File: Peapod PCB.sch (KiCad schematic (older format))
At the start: 17 parts, among them J1 CONN_01X01, J2 CONN_01X02, J3 CONN_01X01, J4 CONN_01X01, J5 CONN_01X01, J6 CONN_01X01, J7 CONN_01X02, U1 ESP8266

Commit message: Updated schematic
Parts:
- removed J3, J4: CONN_01X01, mod:Alligator Pad, symbol CONN_01X01
- added J3: CONN_01X06, Pin_Headers:Pin_Header_Straight_1x06_Pitch2.54mm, symbol CONN_01X06
- R3, R5: footprint (none) -> Resistors_SMD:R_0805_HandSoldering
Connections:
- net +3V3: now also J3.3 (P3)
- net GND: now also J3.1 (P1)
- net at U1.15 (RXD0): now also J3.4 (P4)
- net at U1.16 (TXD0): now also J3.5 (P5)
- no-connect marks 0 -> 2
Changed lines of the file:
@@
 $EndComp
 $Comp
-L GND #PWR5
+L GND #PWR01
 U 1 1 59932223
 P 4850 4225
-F 0 "#PWR5" H 4850 3975 50  0001 C CNN
+F 0 "#PWR01" H 4850 3975 50  0001 C CNN
 F 1 "GND" H 4850 4075 50  0000 C CNN
 F 2 "" H 4850 4225 50  0001 C CNN
@@
 $EndComp
 $Comp
-L GND #PWR6
+L GND #PWR02
 U 1 1 59932907
 P 6800 4100
-F 0 "#PWR6" H 6800 3850 50  0001 C CNN
+F 0 "#PWR02" H 6800 3850 50  0001 C CNN
 F 1 "GND" H 6800 3950 50  0000 C CNN
 F 2 "" H 6800 4100 50  0001 C CNN
@@
 $EndComp
 $Comp
-L GND #PWR1
+L GND #PWR03
 U 1 1 5993357D
 P 4500 3825
-F 0 "#PWR1" H 4500 3575 50  0001 C CNN
+F 0 "#PWR03" H 4500 3575 50  0001 C CNN
 F 1 "GND" H 4500 3675 50  0000 C CNN
 F 2 "" H 4500 3825 50  0001 C CNN
 F 3 "" H 4500 3825 50  0001 C CNN
 	1    4500 3825
-	1    0    0    -1
-$EndComp
-$Comp
-L CONN_01X01 J3
-U 1 1 59933B2D
-P 7450 2875
-F 0 "J3" H 7450 2975 50  0000 C CNN
-F 1 "CONN_01X01" V 7550 2875 50  0000 C CNN
-F 2 "mod:Alligator Pad" H 7450 2875 50  0001 C CNN
-F 3 "" H 7450 2875 50  0001 C CNN
-	1    7450 2875
-	1    0    0    -1
-$EndComp
-$Comp
-L CONN_01X01 J4
-U 1 1 59933BB9
-P 7450 3025
-F 0 "J4" H 7450 3125 50  0000 C CNN
-F 1 "CONN_01X01" V 7550 3025 50  0000 C CNN
-F 2 "mod:Alligator Pad" H 7450 3025 50  0001 C CNN
-F 3 "" H 7450 3025 50  0001 C CNN
-	1    7450 3025
 	1    0    0    -1
 $EndComp
@@
 $EndComp
 $Comp
-L +3.3V #PWR2
+L +3.3V #PWR04
 U 1 1 59933FE4
 P 5300 3175
-F 0 "#PWR2" H 5300 3025 50  0001 C CNN
+F 0 "#PWR04" H 5300 3025 50  0001 C CNN
 F 1 "+3.3V" H 5300 3315 50  0000 C CNN
 F 2 "" H 5300 3175 50  0001 C CNN
@@
 $EndComp
 $Comp
-L +3.3V #PWR4
+L +3.3V #PWR05
 U 1 1 59934256
 P 4950 3925
-F 0 "#PWR4" H 4950 3775 50  0001 C CNN
+F 0 "#PWR05" H 4950 3775 50  0001 C CNN
 F 1 "+3.3V" H 4950 4065 50  0000 C CNN
 F 2 "" H 4950 3925 50  0001 C CNN
@@
 	4500 3775 5050 3775
 Wire Wire Line
-	4500 3475 4500 3625
-Wire Wire Line
-	4500 3625 4500 3775
-Wire Wire Line
-	4500 3775 4500 3825
+	4500 3475 4500 3825
 Connection ~ 4500 3625
 Wire Wire Line
@@
 Wire Wire Line
 	6625 3325 7250 3325
-Wire Wire Line
-	6625 2875 7250 2875
-Wire Wire Line
-	6625 3025 7250 3025
 Wire Wire Line
 	4500 3475 5050 3475
@@
 	4950 4225 4850 4225
 Wire Wire Line
-	5125 2700 5125 2875
-Wire Wire Line
-	5125 2875 5125 3325
+	5125 2700 5125 3325
 Wire Wire Line
 	5125 2875 5325 2875
 Connection ~ 5125 2875
 Wire Wire Line
-	4825 3025 4875 3025
-Wire Wire Line
-	4875 3025 5325 3025
+	4825 3025 5325 3025
 $Comp
 L R R2
@@
 $EndComp
 Wire Wire Line
-	6625 3475 7100 3475
-Wire Wire Line
-	7100 3475 7250 3475
+	6625 3475 7250 3475
 Connection ~ 7100 3475
 $Comp
@@
 $EndComp
 $Comp
-L GND #PWR3
+L GND #PWR06
 U 1 1 599363AF
 P 5325 2700
-F 0 "#PWR3" H 5325 2450 50  0001 C CNN
+F 0 "#PWR06" H 5325 2450 50  0001 C CNN
 F 1 "GND" H 5325 2550 50  0000 C CNN
 F 2 "" H 5325 2700 50  0001 C CNN
@@
 $EndComp
 $Comp
-L +3.3V #PWR7
+L +3.3V #PWR07
 U 1 1 599466C8
 P 7100 3875
-F 0 "#PWR7" H 7100 3725 50  0001 C CNN
+F 0 "#PWR07" H 7100 3725 50  0001 C CNN
 F 1 "+3.3V" H 7100 4015 50  0000 C CNN
 F 2 "" H 7100 3875 50  0001 C CNN
@@
 F 0 "R3" V 6905 3625 50  0000 C CNN
 F 1 "10k" V 6825 3625 50  0000 C CNN
-F 2 "" V 6755 3625 50  0001 C CNN
+F 2 "Resistors_SMD:R_0805_HandSoldering" V 6755 3625 50  0001 C CNN
 F 3 "" H 6825 3625 50  0001 C CNN
 	1    6825 3625
@@
 F 0 "R5" V 6880 3925 50  0000 C CNN
 F 1 "10k" V 6800 3925 50  0000 C CNN
-F 2 "" V 6730 3925 50  0001 C CNN
+F 2 "Resistors_SMD:R_0805_HandSoldering" V 6730 3925 50  0001 C CNN
 F 3 "" H 6800 3925 50  0001 C CNN
 	1    6800 3925
@@
 	6625 3775 6800 3775
 $Comp
-L +3.3V #PWR?
+L +3.3V #PWR08
 U 1 1 59948486
 P 6975 3700
-F 0 "#PWR?" H 6975 3550 50  0001 C CNN
+F 0 "#PWR08" H 6975 3550 50  0001 C CNN
 F 1 "+3.3V" H 6975 3840 50  0000 C CNN
 F 2 "" H 6975 3700 50  0001 C CNN
@@
 	4875 2900 4875 3025
 $Comp
-L GND #PWR?
+L GND #PWR09
 U 1 1 5994872F
 P 4875 2525
-F 0 "#PWR?" H 4875 2275 50  0001 C CNN
+F 0 "#PWR09" H 4875 2275 50  0001 C CNN
 F 1 "GND" H 4875 2375 50  0000 C CNN
 F 2 "" H 4875 2525 50  0001 C CNN
@@
 	4875 2525 4875 2600
 $Comp
-L GND #PWR?
+L GND #PWR010
 U 1 1 599488CC
 P 7250 3750
-F 0 "#PWR?" H 7250 3500 50  0001 C CNN
+F 0 "#PWR010" H 7250 3500 50  0001 C CNN
 F 1 "GND" H 7250 3600 50  0000 C CNN
 F 2 "" H 7250 3750 50  0001 C CNN
@@
 $EndComp
 $Comp
-L GND #PWR?
+L GND #PWR011
 U 1 1 59948924
 P 6625 4000
-F 0 "#PWR?" H 6625 3750 50  0001 C CNN
+F 0 "#PWR011" H 6625 3750 50  0001 C CNN
 F 1 "GND" H 6625 3850 50  0000 C CNN
 F 2 "" H 6625 4000 50  0001 C CNN
@@
 Wire Wire Line
 	5325 3925 4950 3925
+$Comp
+L CONN_01X06 J3
+U 1 1 59947FD8
+P 7500 2450
+F 0 "J3" H 7500 2800 50  0000 C CNN
+F 1 "CONN_01X06" V 7600 2450 50  0000 C CNN
+F 2 "Pin_Headers:Pin_Header_Straight_1x06_Pitch2.54mm" H 7500 2450 50  0001 C CNN
+F 3 "" H 7500 2450 50  0001 C CNN
+	1    7500 2450
+	1    0    0    -1
+$EndComp
+$Comp
+L GND #PWR012
+U 1 1 599480D5
+P 6875 2200
+F 0 "#PWR012" H 6875 1950 50  0001 C CNN
+F 1 "GND" H 6875 2050 50  0000 C CNN
+F 2 "" H 6875 2200 50  0001 C CNN
+F 3 "" H 6875 2200 50  0001 C CNN
+	1    6875 2200
+	0    1    1    0
+$EndComp
+Wire Wire Line
+	6875 2200 7300 2200
+$Comp
+L +3.3V #PWR013
+U 1 1 599481A2
+P 6850 2400
+F 0 "#PWR013" H 6850 2250 50  0001 C CNN
+F 1 "+3.3V" H 6850 2540 50  0000 C CNN
+F 2 "" H 6850 2400 50  0001 C CNN
+F 3 "" H 6850 2400 50  0001 C CNN
+	1    6850 2400
+	0    -1   -1   0
+$EndComp
+Wire Wire Line
+	6850 2400 7300 2400
+Wire Wire Line
+	6625 2875 6800 2875
+Wire Wire Line
+	6800 2875 6800 2600
+Wire Wire Line
+	6800 2600 7300 2600
+Wire Wire Line
+	6625 3025 6625 2500
+Wire Wire Line
+	6625 2500 7300 2500
+NoConn ~ 7300 2700
+NoConn ~ 7300 2300
 $EndSCHEMATC

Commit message: Updated lib
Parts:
- BTN1, BTN3, BTN4: symbol Pushbutton -> Pushbutton-RESCUE-Peapod_PCB
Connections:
- net GND: now also BTN1.~, BTN3.~, BTN4.~; no longer BTN1.1, BTN3.1, BTN4.1
- net at U1.5 (GPIO14): now also BTN4.~; no longer BTN4.2
- net at U1.6 (GPIO12): now also BTN3.~; no longer BTN3.2
- net at U1.7 (GPIO13): now also BTN1.~; no longer BTN1.2
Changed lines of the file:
@@
 EESchema Schematic File Version 2
+LIBS:Peapod PCB-rescue
 LIBS:power
 LIBS:device
@@
 $EndComp
 $Comp
-L Pushbutton BTN1
+L Pushbutton-RESCUE-Peapod_PCB BTN1
 U 1 1 5993320C
 P 5150 3775
@@
 $EndComp
 $Comp
-L Pushbutton BTN3
+L Pushbutton-RESCUE-Peapod_PCB BTN3
 U 1 1 599332EE
 P 4775 3625
@@
 $EndComp
 $Comp
-L Pushbutton BTN4
+L Pushbutton-RESCUE-Peapod_PCB BTN4
 U 1 1 5993333F
 P 5150 3475

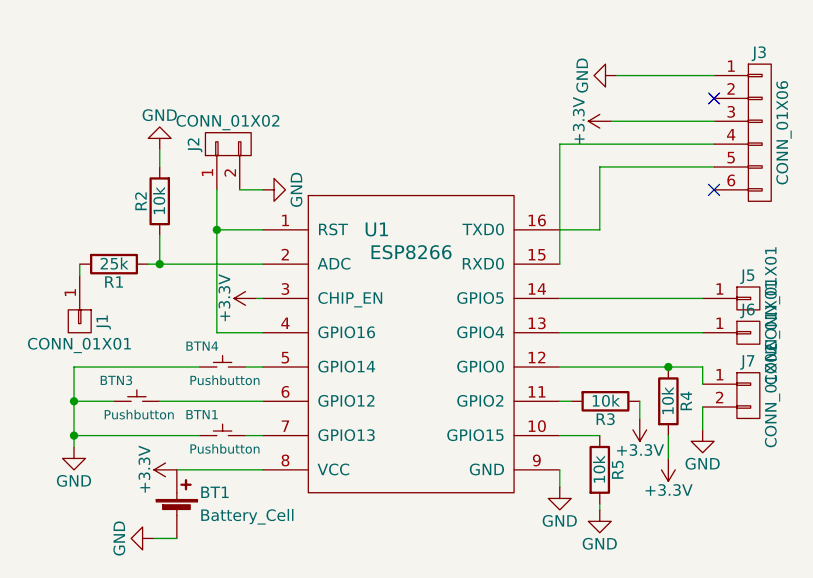
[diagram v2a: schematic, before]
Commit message: updated pushbutton
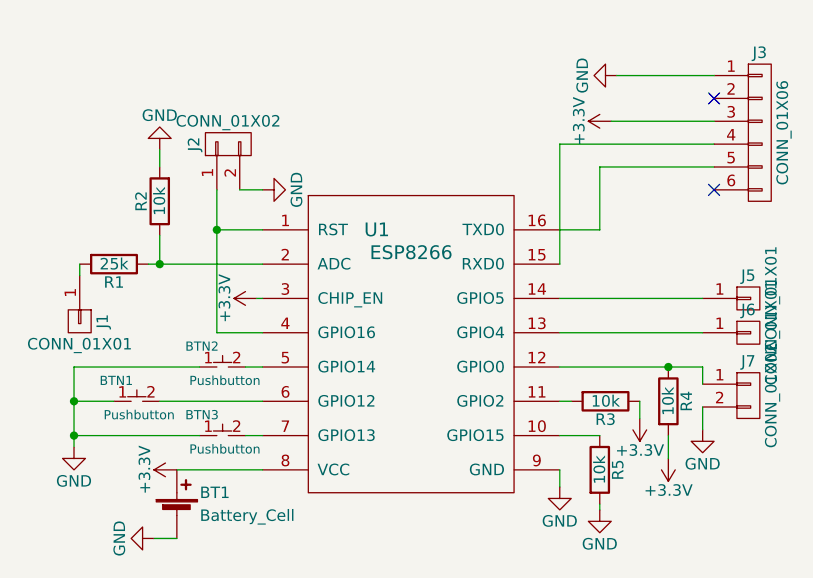
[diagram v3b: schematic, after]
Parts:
- removed BTN1, BTN3, BTN4: Pushbutton, mod:Pushbutton, symbol Pushbutton-RESCUE-Peapod_PCB
- added BTN1, BTN2, BTN3: Pushbutton, mod:Pushbutton, symbol Pushbutton
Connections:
- net GND: now also BTN1.1, BTN2.1, BTN3.1
- net at U1.5 (GPIO14): now also BTN2.2
- net at U1.6 (GPIO12): now also BTN1.2
- net at U1.7 (GPIO13): now also BTN3.2
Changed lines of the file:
@@
-$EndComp
-$Comp
-L Pushbutton-RESCUE-Peapod_PCB BTN1
-U 1 1 5993320C
-P 5150 3775
-F 0 "BTN1" H 5060 3865 40  0000 C CNN
-F 1 "Pushbutton" H 5160 3715 40  0000 C CNN
-F 2 "mod:Pushbutton" H 4850 3375 60  0001 C CNN
-F 3 "" H 4850 3375 60  0001 C CNN
-	1    5150 3775
-	1    0    0    -1
-$EndComp
-$Comp
-L Pushbutton-RESCUE-Peapod_PCB BTN3
-U 1 1 599332EE
-P 4775 3625
-F 0 "BTN3" H 4685 3715 40  0000 C CNN
-F 1 "Pushbutton" H 4785 3565 40  0000 C CNN
-F 2 "mod:Pushbutton" H 4475 3225 60  0001 C CNN
-F 3 "" H 4475 3225 60  0001 C CNN
-	1    4775 3625
-	1    0    0    -1
-$EndComp
-$Comp
-L Pushbutton-RESCUE-Peapod_PCB BTN4
-U 1 1 5993333F
-P 5150 3475
-F 0 "BTN4" H 5060 3565 40  0000 C CNN
-F 1 "Pushbutton" H 5160 3415 40  0000 C CNN
-F 2 "mod:Pushbutton" H 4850 3075 60  0001 C CNN
-F 3 "" H 4850 3075 60  0001 C CNN
-	1    5150 3475
-	1    0    0    -1
 $EndComp
 $Comp
@@
 NoConn ~ 7300 2700
 NoConn ~ 7300 2300
+$Comp
+L Pushbutton BTN2
+U 1 1 5994A123
+P 5150 3475
+F 0 "BTN2" H 5060 3565 40  0000 C CNN
+F 1 "Pushbutton" H 5160 3415 40  0000 C CNN
+F 2 "mod:Pushbutton" H 4850 3075 60  0001 C CNN
+F 3 "" H 4850 3075 60  0001 C CNN
+	1    5150 3475
+	1    0    0    -1
+$EndComp
+$Comp
+L Pushbutton BTN1
+U 1 1 5994A192
+P 4775 3625
+F 0 "BTN1" H 4685 3715 40  0000 C CNN
+F 1 "Pushbutton" H 4785 3565 40  0000 C CNN
+F 2 "mod:Pushbutton" H 4475 3225 60  0001 C CNN
+F 3 "" H 4475 3225 60  0001 C CNN
+	1    4775 3625
+	1    0    0    -1
+$EndComp
+$Comp
+L Pushbutton BTN3
+U 1 1 5994A1EB
+P 5150 3775
+F 0 "BTN3" H 5060 3865 40  0000 C CNN
+F 1 "Pushbutton" H 5160 3715 40  0000 C CNN
+F 2 "mod:Pushbutton" H 4850 3375 60  0001 C CNN
+F 3 "" H 4850 3375 60  0001 C CNN
+	1    5150 3775
+	1    0    0    -1
+$EndComp
 $EndSCHEMATC

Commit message: Changed schematic
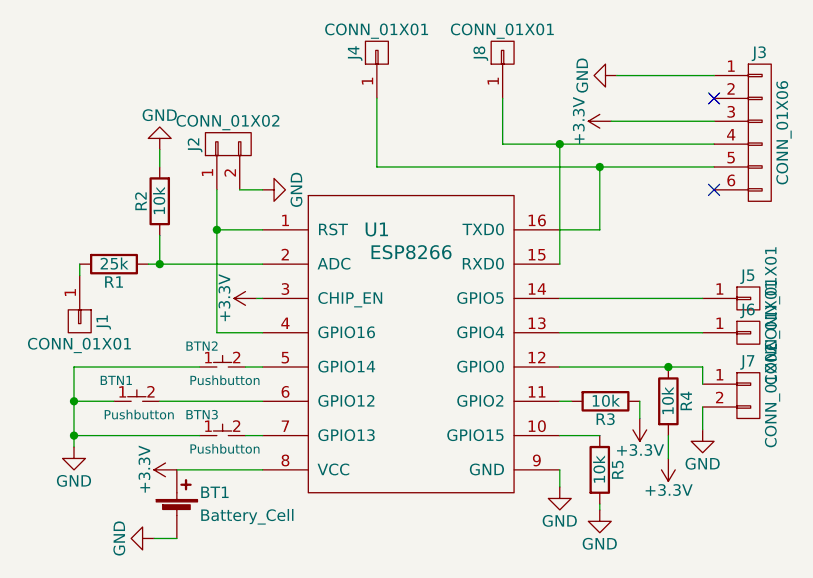
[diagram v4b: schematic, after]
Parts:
- added J4, J8: CONN_01X01, symbol CONN_01X01
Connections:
- net at J3.4 (P4), U1.15 (RXD0): now also J8.1 (P1)
- net at J3.5 (P5), U1.16 (TXD0): now also J4.1 (P1)
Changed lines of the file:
@@
 $EndComp
 $Comp
-L GND #PWR01
+L GND #PWR2
 U 1 1 59932223
 P 4850 4225
-F 0 "#PWR01" H 4850 3975 50  0001 C CNN
+F 0 "#PWR2" H 4850 3975 50  0001 C CNN
 F 1 "GND" H 4850 4075 50  0000 C CNN
 F 2 "" H 4850 4225 50  0001 C CNN
@@
 $EndComp
 $Comp
-L GND #PWR02
+L GND #PWR8
 U 1 1 59932907
 P 6800 4100
-F 0 "#PWR02" H 6800 3850 50  0001 C CNN
+F 0 "#PWR8" H 6800 3850 50  0001 C CNN
 F 1 "GND" H 6800 3950 50  0000 C CNN
 F 2 "" H 6800 4100 50  0001 C CNN
@@
 $EndComp
 $Comp
-L GND #PWR03
+L GND #PWR1
 U 1 1 5993357D
 P 4500 3825
-F 0 "#PWR03" H 4500 3575 50  0001 C CNN
+F 0 "#PWR1" H 4500 3575 50  0001 C CNN
 F 1 "GND" H 4500 3675 50  0000 C CNN
 F 2 "" H 4500 3825 50  0001 C CNN
@@
 $EndComp
 $Comp
-L +3.3V #PWR04
+L +3.3V #PWR5
 U 1 1 59933FE4
 P 5300 3175
-F 0 "#PWR04" H 5300 3025 50  0001 C CNN
+F 0 "#PWR5" H 5300 3025 50  0001 C CNN
 F 1 "+3.3V" H 5300 3315 50  0000 C CNN
 F 2 "" H 5300 3175 50  0001 C CNN
@@
 $EndComp
 $Comp
-L +3.3V #PWR05
+L +3.3V #PWR4
 U 1 1 59934256
 P 4950 3925
-F 0 "#PWR05" H 4950 3775 50  0001 C CNN
+F 0 "#PWR4" H 4950 3775 50  0001 C CNN
 F 1 "+3.3V" H 4950 4065 50  0000 C CNN
 F 2 "" H 4950 3925 50  0001 C CNN
@@
 	4500 3775 5050 3775
 Wire Wire Line
-	4500 3475 4500 3825
+	4500 3475 4500 3625
+Wire Wire Line
+	4500 3625 4500 3775
+Wire Wire Line
+	4500 3775 4500 3825
 Connection ~ 4500 3625
 Wire Wire Line
@@
 	4950 4225 4850 4225
 Wire Wire Line
-	5125 2700 5125 3325
+	5125 2700 5125 2875
+Wire Wire Line
+	5125 2875 5125 3325
 Wire Wire Line
 	5125 2875 5325 2875
 Connection ~ 5125 2875
 Wire Wire Line
-	4825 3025 5325 3025
+	4825 3025 4875 3025
+Wire Wire Line
+	4875 3025 5325 3025
 $Comp
 L R R2
@@
 $EndComp
 Wire Wire Line
-	6625 3475 7250 3475
+	6625 3475 7100 3475
+Wire Wire Line
+	7100 3475 7250 3475
 Connection ~ 7100 3475
 $Comp
@@
 $EndComp
 $Comp
-L GND #PWR06
+L GND #PWR6
 U 1 1 599363AF
 P 5325 2700
-F 0 "#PWR06" H 5325 2450 50  0001 C CNN
+F 0 "#PWR6" H 5325 2450 50  0001 C CNN
 F 1 "GND" H 5325 2550 50  0000 C CNN
 F 2 "" H 5325 2700 50  0001 C CNN
@@
 $EndComp
 $Comp
-L +3.3V #PWR07
+L +3.3V #PWR12
 U 1 1 599466C8
 P 7100 3875
-F 0 "#PWR07" H 7100 3725 50  0001 C CNN
+F 0 "#PWR12" H 7100 3725 50  0001 C CNN
 F 1 "+3.3V" H 7100 4015 50  0000 C CNN
 F 2 "" H 7100 3875 50  0001 C CNN
@@
 	6625 3775 6800 3775
 $Comp
-L +3.3V #PWR08
+L +3.3V #PWR11
 U 1 1 59948486
 P 6975 3700
-F 0 "#PWR08" H 6975 3550 50  0001 C CNN
+F 0 "#PWR11" H 6975 3550 50  0001 C CNN
 F 1 "+3.3V" H 6975 3840 50  0000 C CNN
 F 2 "" H 6975 3700 50  0001 C CNN
@@
 	4875 2900 4875 3025
 $Comp
-L GND #PWR09
+L GND #PWR3
 U 1 1 5994872F
 P 4875 2525
-F 0 "#PWR09" H 4875 2275 50  0001 C CNN
+F 0 "#PWR3" H 4875 2275 50  0001 C CNN
 F 1 "GND" H 4875 2375 50  0000 C CNN
 F 2 "" H 4875 2525 50  0001 C CNN
@@
 	4875 2525 4875 2600
 $Comp
-L GND #PWR010
+L GND #PWR13
 U 1 1 599488CC
 P 7250 3750
-F 0 "#PWR010" H 7250 3500 50  0001 C CNN
+F 0 "#PWR13" H 7250 3500 50  0001 C CNN
 F 1 "GND" H 7250 3600 50  0000 C CNN
 F 2 "" H 7250 3750 50  0001 C CNN
@@
 $EndComp
 $Comp
-L GND #PWR011
+L GND #PWR7
 U 1 1 59948924
 P 6625 4000
-F 0 "#PWR011" H 6625 3750 50  0001 C CNN
+F 0 "#PWR7" H 6625 3750 50  0001 C CNN
 F 1 "GND" H 6625 3850 50  0000 C CNN
 F 2 "" H 6625 4000 50  0001 C CNN
@@
 $EndComp
 $Comp
-L GND #PWR012
+L GND #PWR10
 U 1 1 599480D5
 P 6875 2200
-F 0 "#PWR012" H 6875 1950 50  0001 C CNN
+F 0 "#PWR10" H 6875 1950 50  0001 C CNN
 F 1 "GND" H 6875 2050 50  0000 C CNN
 F 2 "" H 6875 2200 50  0001 C CNN
@@
 	6875 2200 7300 2200
 $Comp
-L +3.3V #PWR013
+L +3.3V #PWR9
 U 1 1 599481A2
 P 6850 2400
-F 0 "#PWR013" H 6850 2250 50  0001 C CNN
+F 0 "#PWR9" H 6850 2250 50  0001 C CNN
 F 1 "+3.3V" H 6850 2540 50  0000 C CNN
 F 2 "" H 6850 2400 50  0001 C CNN
@@
 	6800 2875 6800 2600
 Wire Wire Line
+	6800 2600 6800 2600
+Wire Wire Line
 	6800 2600 7300 2600
 Wire Wire Line
 	6625 3025 6625 2500
+Wire Wire Line
+	6375 2500 6625 2500
 Wire Wire Line
 	6625 2500 7300 2500
@@
 	1    0    0    -1
 $EndComp
+$Comp
+L CONN_01X01 J4
+U 1 1 5995C3B2
+P 5825 2100
+F 0 "J4" H 5825 2200 50  0000 C CNN
+F 1 "CONN_01X01" V 5925 2100 50  0000 C CNN
+F 2 "" H 5825 2100 50  0001 C CNN
+F 3 "" H 5825 2100 50  0001 C CNN
+	1    5825 2100
+	0    -1   -1   0
+$EndComp
+$Comp
+L CONN_01X01 J8
+U 1 1 5995C3FF
+P 6375 2100
+F 0 "J8" H 6375 2200 50  0000 C CNN
+F 1 "CONN_01X01" V 6475 2100 50  0000 C CNN
+F 2 "" H 6375 2100 50  0001 C CNN
+F 3 "" H 6375 2100 50  0001 C CNN
+	1    6375 2100
+	0    -1   -1   0
+$EndComp
+Wire Wire Line
+	6375 2500 6375 2300
+Connection ~ 6625 2500
+Wire Wire Line
+	6800 2600 5825 2600
+Wire Wire Line
+	5825 2600 5825 2300
+Connection ~ 6800 2600
 $EndSCHEMATC
